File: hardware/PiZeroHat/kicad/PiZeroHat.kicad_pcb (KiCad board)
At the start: 2 copper layers, 65 x 30 mm, 1 part

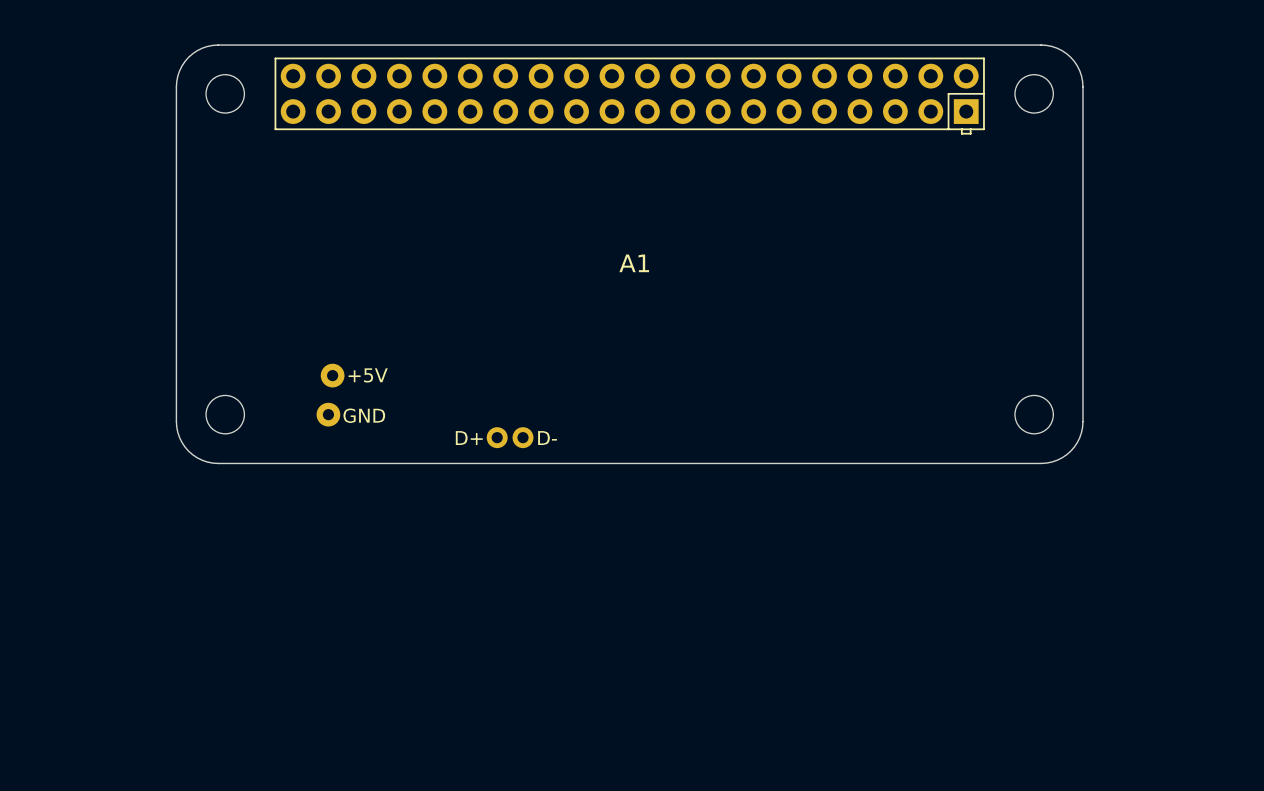
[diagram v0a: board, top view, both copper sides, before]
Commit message: chore(hardware): replace stale PiZeroHat with current design; drop old boards
- Remove hardware/smarttread/ and hardware/st2/ (superseded in-house
  treadmill-adapter iterations; history retains them).
- Replace the stale Mar-7 hardware/PiZeroHat/ snapshot with the current
  May-12 design (SHA-verified identical to the canonical working copy).
  Vendored clean: design sources + lib + gerbers + wiring docs +
  LICENSE; excluded .history/ (39M), backups, fp-info-cache, tmp/,
  *.bak/*.lck/*.prl/*.rpt. Verified content: D24V10F5 buck + RJ45
  To-Motor/From-Console connectors.

Co-Authored-By: Claude Opus 4.7 (1M context) <noreply@anthropic.com>
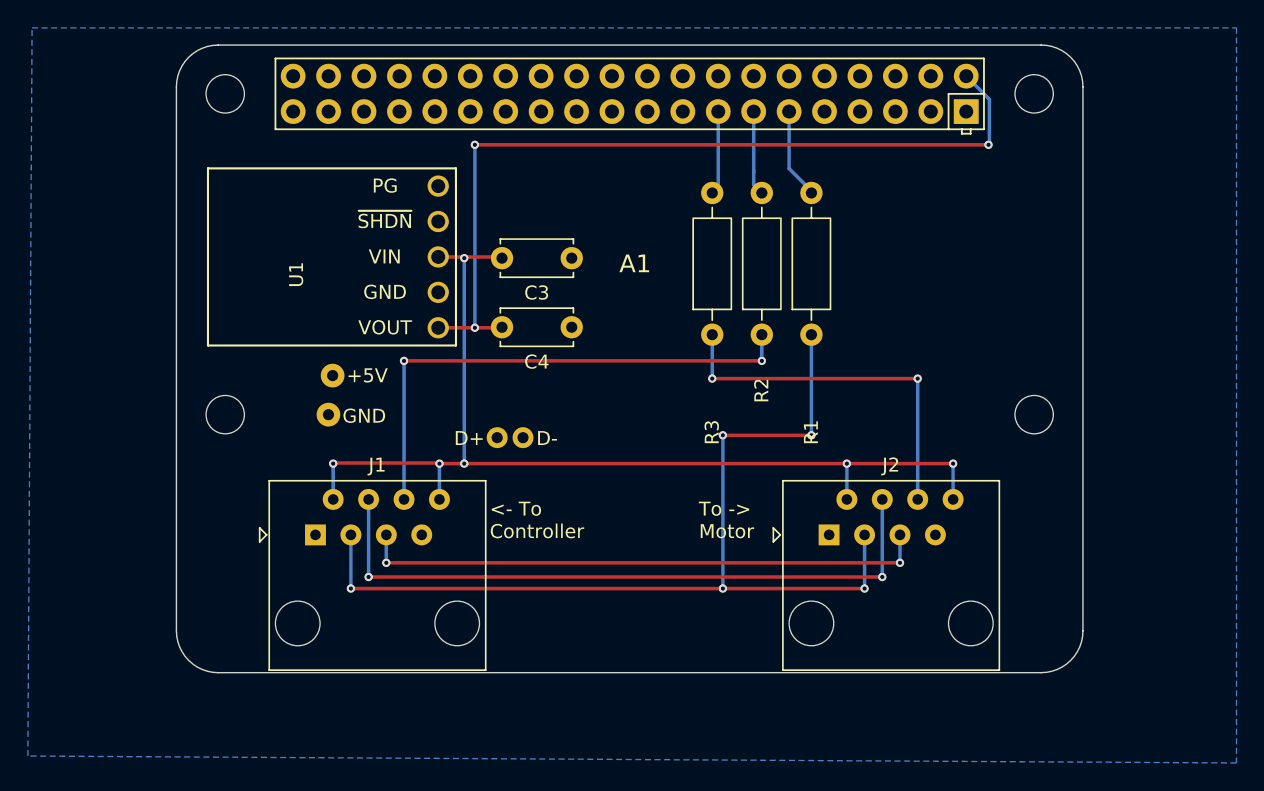
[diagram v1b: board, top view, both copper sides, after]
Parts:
- added C3: 100nF, Capacitor_THT:C_Disc_D5.0mm_W2.5mm_P5.00mm, F.Cu at (147.3, 94.4)
- added C4: 100nF, Capacitor_THT:C_Disc_D5.0mm_W2.5mm_P5.00mm, F.Cu at (147.3, 99.3)
- added J1: From Console, Connector_RJ:RJ45_Amphenol_54602-x08_Horizontal, F.Cu at (129.0, 114.2)
- added J2: To Motor, Connector_RJ:RJ45_Amphenol_54602-x08_Horizontal, F.Cu at (165.8, 114.2)
- added R1: 100, Resistor_THT:R_Axial_DIN0207_L6.3mm_D2.5mm_P10.16mm_Horizontal, F.Cu at (164.5, 99.9)
- added R2: 100, Resistor_THT:R_Axial_DIN0207_L6.3mm_D2.5mm_P10.16mm_Horizontal, F.Cu at (161.0, 99.9)
- added R3: 100, Resistor_THT:R_Axial_DIN0207_L6.3mm_D2.5mm_P10.16mm_Horizontal, F.Cu at (157.4, 99.9)
- added U1: D24V10F5, Scott:D24V10F5, F.Cu at (139.0, 100.6)
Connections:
- A1 pad 11: unconnected-(A1-GP17-Pad11) -> Net-(A1-GP17)
- A1 pad 13: unconnected-(A1-GP27-Pad13) -> Net-(A1-GP27)
- A1 pad 14: unconnected-(A1-GND-Pad14) -> GND
- A1 pad 15: unconnected-(A1-GP22-Pad15) -> Net-(A1-GP22)
- A1 pad 2: unconnected-(A1-+5V-Pad2) -> Net-(U1-VOUT)
- A1 pad 20: unconnected-(A1-GND-Pad20) -> GND
- A1 pad 25: unconnected-(A1-GND-Pad25) -> GND
- A1 pad 30: unconnected-(A1-GND-Pad30) -> GND
- A1 pad 34: unconnected-(A1-GND-Pad34) -> GND
- A1 pad 39: unconnected-(A1-GND-Pad39) -> GND
- A1 pad 6: unconnected-(A1-GND-Pad6) -> GND
- A1 pad 9: unconnected-(A1-GND-Pad9) -> GND
- A1 pad PP6: unconnected-(A1-GND-PadPP6) -> GND
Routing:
- net +8V: track 0.00 -> 74.4 mm, vias 0 -> 6
- net Net-(J1-Pad3): track 0.00 -> 69.2 mm, vias 0 -> 5
- net Net-(U1-VOUT): track 0.00 -> 61.4 mm, vias 0 -> 3
- net Net-(J1-Pad4): track 0.00 -> 48.2 mm, vias 0 -> 2
- net Net-(J1-Pad5): track 0.00 -> 40.8 mm, vias 0 -> 2
- net Net-(J1-Pad6): track 0.00 -> 37.5 mm, vias 0 -> 2
- net Net-(J2-Pad6): track 0.00 -> 25.5 mm, vias 0 -> 2
- net Net-(A1-GP17): track 0.00 -> 7.21 mm
- net Net-(A1-GP22): track 0.00 -> 6.32 mm
- net Net-(A1-GP27): track 0.00 -> 6.29 mm
- added copper zone on B.Cu, net GND
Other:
- board size 65 x 30 mm -> 65 x 45 mm
- board text added: "<- To Controller"
- board text added: "To -> Motor"
